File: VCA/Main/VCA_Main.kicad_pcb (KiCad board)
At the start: 2 copper layers, 29.5 x 62.7 mm, 35 parts, among them J1 Power, J10 IO_B, J11 IO_Power, J5 IO_A, U1 AS3360, U2 TL072, U3 TL072, U4 TL072

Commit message: Clean up VCA boards
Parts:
- added C4: C, Capacitor_SMD:C_0805_2012Metric, F.Cu at (85.1, 132.1)
- added C5: C, Capacitor_SMD:C_0805_2012Metric, F.Cu at (72.6, 130.0)
- added R25: R_US, Resistor_SMD:R_0805_2012Metric, F.Cu at (87.9, 127.8)
- added R26: R_US, Resistor_SMD:R_0805_2012Metric, F.Cu at (88.1, 132.1)
- added R27: R_US, Resistor_SMD:R_0805_2012Metric, F.Cu at (69.6, 129.8)
- added R28: R_US, Resistor_SMD:R_0805_2012Metric, F.Cu at (69.6, 131.8)
- added REF**: OSHW-Logo2_7.3x6mm_SilkScreen, Symbol:OSHW-Logo2_7.3x6mm_SilkScreen, B.Cu at (88.1, 84.3)
- moved R24 4.65 mm to (86.0, 136.4)
- moved R23 2.54 mm to (72.1, 135.6), turned to 180 degrees
- moved J10 0.63 mm to (91.4, 106.7)
- moved R6 0.51 mm to (87.9, 114.6)
- moved R5 0.25 mm to (87.9, 111.5)
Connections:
- U4 pad 1: /Out_A -> Net-(C5-Pad1)
- U4 pad 2: /Out_A -> Net-(C5-Pad2)
- U4 pad 6: /Out_B -> Net-(C4-Pad2)
- U4 pad 7: /Out_B -> Net-(C4-Pad1)
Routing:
- net Net-(C4-Pad1): track 0.00 -> 6.54 mm
- net /Out_A: track 12.4 -> 5.91 mm
- net /Out_B: track 12.7 -> 6.55 mm
- net Net-(C4-Pad2): track 0.00 -> 5.68 mm
- net Net-(C5-Pad2): track 0.00 -> 5.14 mm
- net Net-(C5-Pad1): track 0.00 -> 5.07 mm
- net Net-(R24-Pad1): track 34.0 -> 30.4 mm
- net Net-(R23-Pad1): track 30.6 -> 28.4 mm
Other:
- board text added: "A"
- board text added: "B"
- board text added: "IO Pwr"
- board text added: "VCA Main Board Rev 2"
- board text added: "WH"

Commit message: Bunch of bug fixes and tweaks
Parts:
- added C6: C, Capacitor_SMD:C_0805_2012Metric, F.Cu at (66.3, 83.6)
- added C7: C, Capacitor_SMD:C_0805_2012Metric, F.Cu at (82.3, 85.2)
- added C8: C, Capacitor_SMD:C_0805_2012Metric, F.Cu at (74.9, 100.8)
- added C9: C, Capacitor_SMD:C_0805_2012Metric, F.Cu at (91.2, 83.3)
- added H1: Top_MH1, Eurorack:eurorack_mounting_hole, F.Cu at (66.7, 78.7)
- added H2: Bottom_MH1, Eurorack:eurorack_mounting_hole, F.Cu at (66.7, 135.9)
- added H3: Top_MH2, Eurorack:eurorack_mounting_hole, F.Cu at (90.8, 78.7)
- added H4: Bottom_MH2, Eurorack:eurorack_mounting_hole, F.Cu at (90.8, 135.9)
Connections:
- J11 pad 3: (no net) -> Net-(J11-Pad3)
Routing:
- net Net-(C7-Pad2): track 28.8 -> 35.1 mm
- net Net-(C8-Pad2): track 14.4 -> 20.0 mm
- net Net-(C6-Pad1): track 9.87 -> 14.8 mm
- net Net-(C8-Pad1): track 11.8 -> 15.7 mm
- net Net-(C6-Pad2): track 30.9 -> 34.2 mm
- net Net-(C7-Pad1): track 6.27 -> 9.18 mm
- net Net-(C9-Pad2): track 13.4 -> 15.7 mm
- net Net-(C9-Pad1): track 16.6 -> 18.9 mm
- net GNDREF: vias 6 -> 2

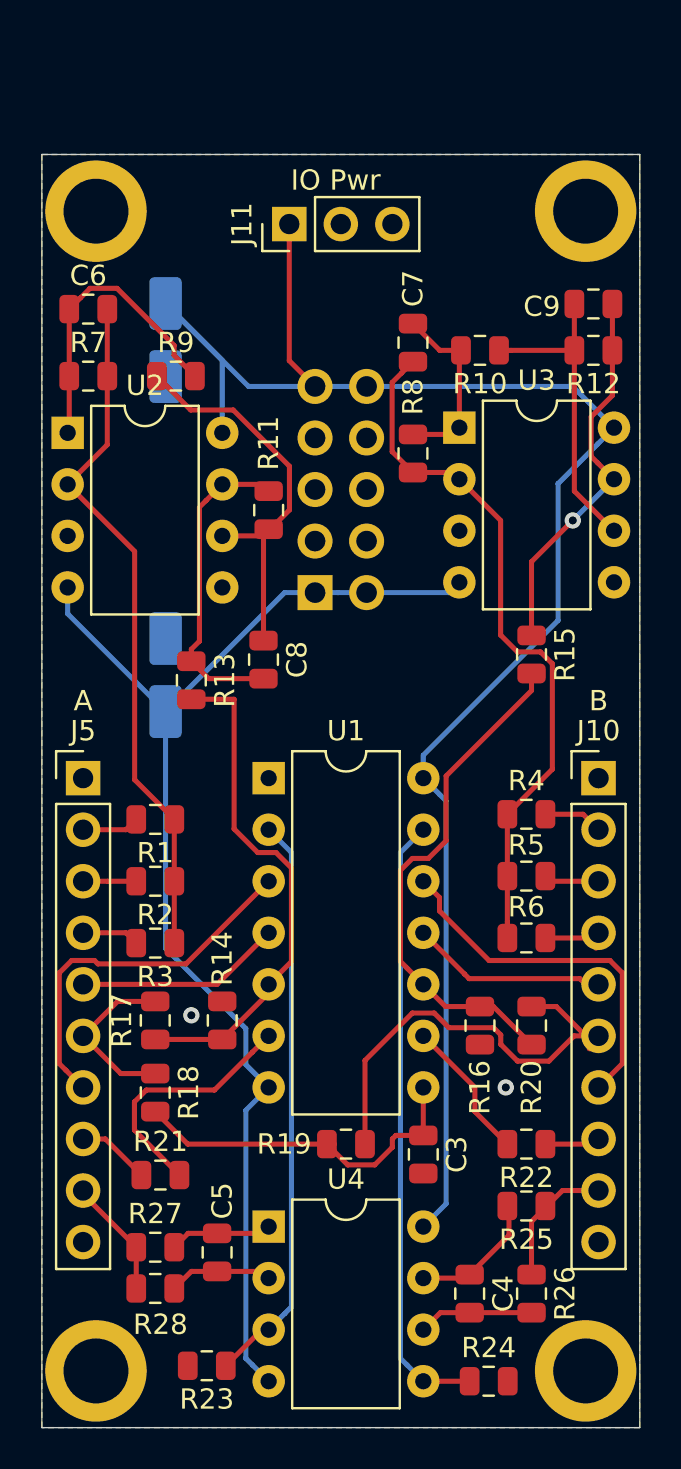
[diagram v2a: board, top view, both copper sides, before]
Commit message: Clean up layout of VCA board
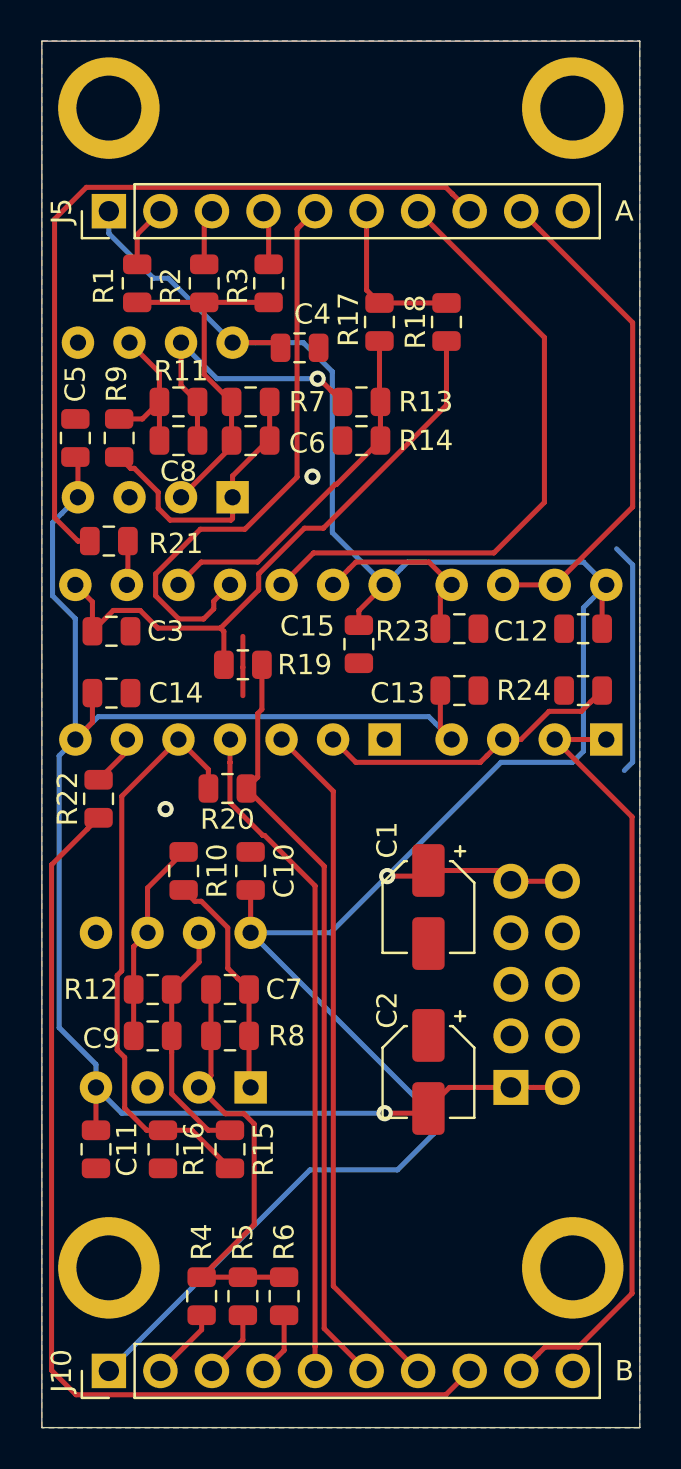
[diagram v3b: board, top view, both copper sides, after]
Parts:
- removed J11: IO_Power, Connector_PinHeader_2.54mm:PinHeader_1x03_P2.54mm_Vertical
- removed R25, R26, R27, R28: R_US, Resistor_SMD:R_0805_2012Metric
- added C10: 0.1uF, Capacitor_SMD:C_0805_2012Metric, F.Cu at (74.3, 111.3)
- added C11: 0.1uF, Capacitor_SMD:C_0805_2012Metric, F.Cu at (66.7, 125.0)
- added C12: 0.1uF, Capacitor_SMD:C_0805_2012Metric, F.Cu at (90.7, 99.3)
- added C13: 0.1uF, Capacitor_SMD:C_0805_2012Metric, F.Cu at (84.6, 102.4)
- added C14: 0.1uF, Capacitor_SMD:C_0805_2012Metric, F.Cu at (67.4, 102.5)
- added C15: 0.1uF, Capacitor_SMD:C_0805_2012Metric, F.Cu at (79.6, 100.1)
- C1, C2: moved to F.Cu
- C4, C5: value C -> 0.1uF
- U1, U2, U3, U4: moved to B.Cu
- moved C4 47.4 mm to (76.7, 85.5), turned to 180 degrees
- moved C9 42.1 mm to (69.5, 119.4)
- moved C5 40.7 mm to (65.7, 89.9)
- moved R18 40.6 mm to (83.9, 84.2)
- moved R23 38.4 mm to (84.6, 99.3), turned to 0 degrees
- moved R12 38.3 mm to (69.5, 117.1)
- moved J10 37.9 mm to (67.3, 135.9), turned to 90 degrees
- moved R17 36.1 mm to (80.6, 84.2)
- moved R24 34.4 mm to (90.7, 102.4), turned to 180 degrees
- moved U3 34.1 mm to (74.3, 121.9), turned to 90 degrees
- moved C7 33.1 mm to (73.3, 117.1), turned to 180 degrees
- moved R3 33.0 mm to (75.2, 82.3), turned to 90 degrees
- moved R21 31.3 mm to (67.3, 95.0)
- moved C1 30.8 mm to (83.1, 113.0)
- moved R8 30.1 mm to (73.3, 119.4), turned to 180 degrees
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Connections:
- C4 pad 1: Net-(C4-Pad1) -> GNDREF
- C4 pad 2: Net-(C4-Pad2) -> +12V
- C5 pad 1: Net-(C5-Pad1) -> GNDREF
- C5 pad 2: Net-(C5-Pad2) -> -12V
- J10 pad 1: GNDREF -> +12V
- J5 pad 1: GNDREF -> +12V
- U1 pad 10: Net-(R15-Pad2) -> Net-(R13-Pad2)
- U1 pad 11: /SW_Lin_B -> /SW_Lin_A
- U1 pad 12: /SW_Com_B -> /SW_Com_A
- U1 pad 13: Net-(R24-Pad1) -> Net-(R23-Pad1)
- U1 pad 2: Net-(R23-Pad1) -> Net-(R24-Pad1)
- U1 pad 3: /SW_Com_A -> /SW_Com_B
- U1 pad 4: /SW_Lin_A -> /SW_Lin_B
- U1 pad 5: Net-(R13-Pad2) -> Net-(R15-Pad2)
- U1 pad 6: Net-(R21-Pad2) -> Net-(R22-Pad2)
- U1 pad 9: Net-(R22-Pad2) -> Net-(R21-Pad2)
- U4 pad 1: Net-(C5-Pad1) -> /Out_B
- U4 pad 2: Net-(C5-Pad2) -> /Out_B
- U4 pad 3: Net-(R23-Pad1) -> Net-(R24-Pad1)
- U4 pad 5: Net-(R24-Pad1) -> Net-(R23-Pad1)
- U4 pad 6: Net-(C4-Pad2) -> /Out_A
- U4 pad 7: Net-(C4-Pad1) -> /Out_A
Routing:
- net /In_B: track 2.78 -> 49.8 mm
- net +12V: track 84.9 -> 119.9 mm, vias 0 -> 1
- net /In_A: track 3.61 -> 38.5 mm
- net /Out_B: track 6.55 -> 38.5 mm
- net /SW_Lin_B: track 9.95 -> 32.9 mm
- net -12V: track 61.3 -> 84.1 mm, vias 0 -> 1
- net Net-(R23-Pad1): track 28.4 -> 9.16 mm
- net /Out_A: track 5.91 -> 24.8 mm
- net /SW_Lin_A: track 10.2 -> 28.6 mm
- net Net-(C6-Pad2): track 34.2 -> 17.7 mm
- net /SW_Com_B: track 18.2 -> 33.9 mm
- net Net-(R24-Pad1): track 30.4 -> 15.2 mm
- net /SW_Log_B: track 23.0 -> 37.6 mm
- net GNDREF: track 0.18 -> 14.3 mm
- net Net-(C7-Pad2): track 35.1 -> 21.4 mm
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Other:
- board size 29.5 x 62.7 mm -> 29.5 x 68.3 mm
- board text removed: "IO Pwr"
